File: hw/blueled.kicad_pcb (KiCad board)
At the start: 2 copper layers, 54 x 85.6 mm, 58 parts, among them J1 Barrel_Jack, J2 LED Strip, J3 ICSP, J4 Screw_Terminal_01x02, Q1 Q_PMOS_SDG, Q2 Q_PNP_EBC, SW2 PUSH, U1 ATmega328P-AU, U2 HC-05, U3 AMS1117-3.3, U4 AT25SF081, U5 LM25085MM, X1 CSTCE

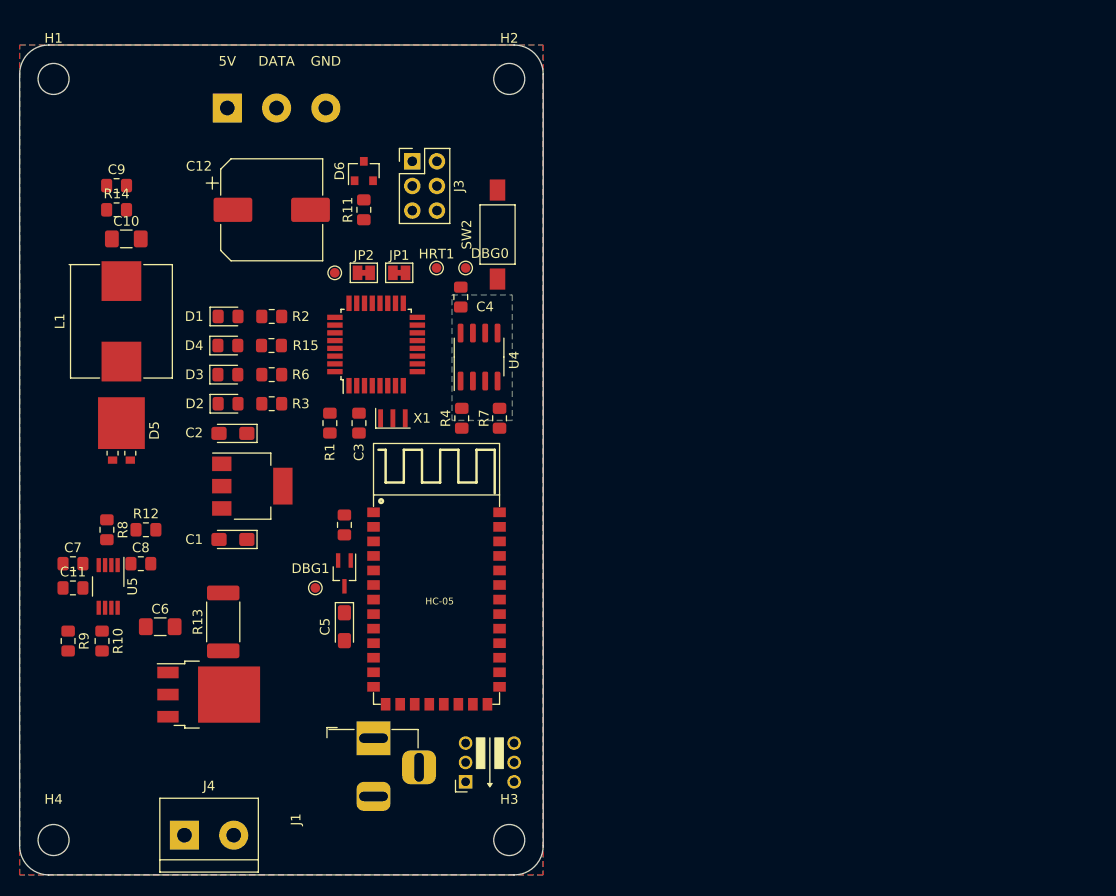
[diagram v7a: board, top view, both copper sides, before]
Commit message: add(hw): a lot of progress in layouting + bug fixes
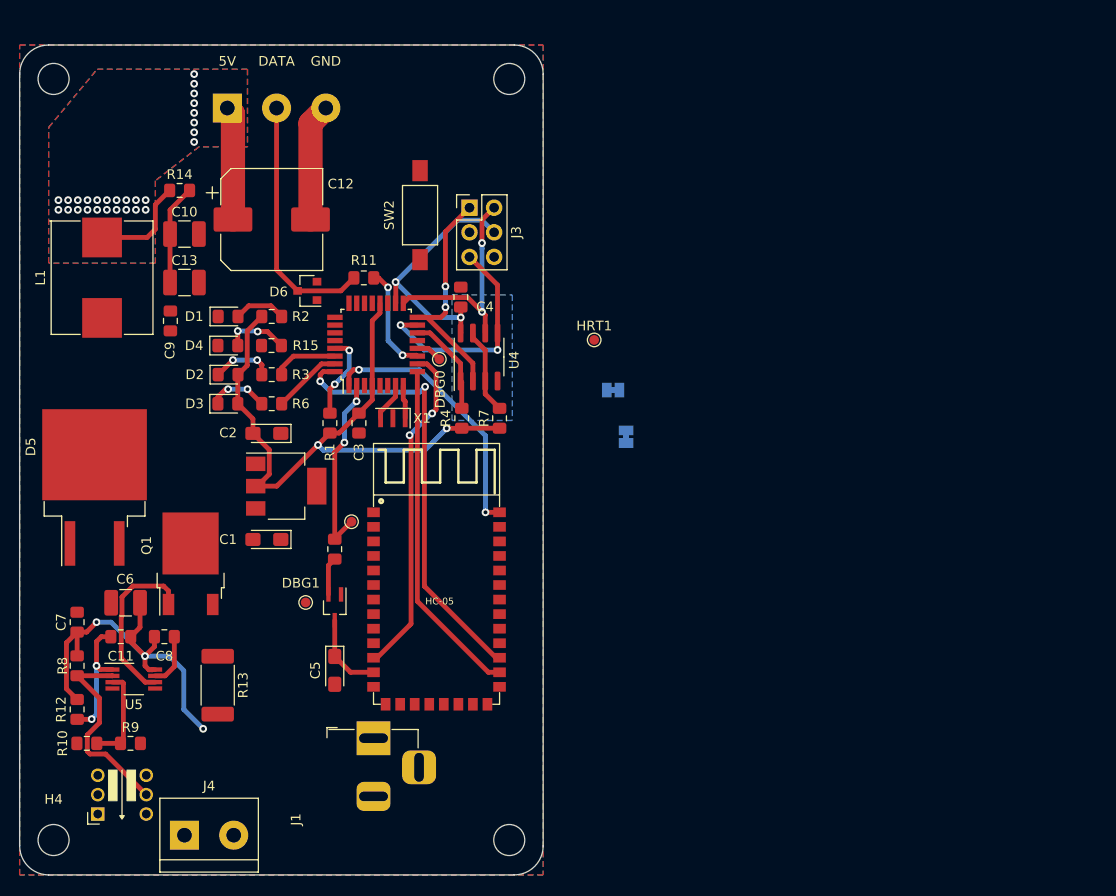
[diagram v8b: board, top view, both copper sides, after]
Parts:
- added C13: 47uF, Capacitor_SMD:C_1210_3225Metric_Pad1.42x2.65mm_HandSolder, F.Cu at (137.0, 87.5)
- C10: value 100uF -> 47uF; footprint Capacitor_SMD:C_1206_3216Metric_Pad1.42x1.75mm_HandSolder -> Capacitor_SMD:C_1210_3225Metric_Pad1.42x2.65mm_HandSolder
- C6: footprint Capacitor_SMD:C_1206_3216Metric_Pad1.42x1.75mm_HandSolder -> Capacitor_SMD:C_1210_3225Metric_Pad1.42x2.65mm_HandSolder
- C9: value 0.1uF -> 4700pF
- D5: footprint Diode_SMD:D_Powermite3 -> Package_TO_SOT_SMD:TO-263-3_TabPin2
- JP1, JP2: moved to B.Cu
- R14: value 10k -> 0.27
- moved S1 38.1 mm to (130.6, 140.3)
- moved JP2 31.9 mm to (182.6, 103.4), turned to 90 degrees
- moved DBG2 25.7 mm to (154.2, 112.2)
- moved JP1 25.2 mm to (181.2, 98.6)
- moved R12 19.8 mm to (125.9, 131.5), turned to 90 degrees
- moved HRT1 17.9 mm to (179.3, 93.4)
- moved C9 15.0 mm to (135.6, 91.5), turned to 90 degrees
- moved R8 14.4 mm to (125.9, 127.0)
- moved D6 13.7 mm to (149.7, 88.4), turned to 180 degrees
- moved Q1 13.6 mm to (137.6, 116.5), turned to 90 degrees
- moved R9 12.4 mm to (131.4, 135.0), turned to 0 degrees
- moved R10 10.7 mm to (126.9, 135.0), turned to 0 degrees
- moved U5 9.91 mm to (131.8, 128.4), turned to 0 degrees
- moved DBG0 9.79 mm to (163.3, 95.4)
- moved SW2 8.24 mm to (161.3, 80.5)
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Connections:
- C12 pad 1: (no net) -> +5V
- Q1 pad 1: Net-(D5-Pad1) -> Net-(Q1-Pad1)
- Q1 pad 2: Net-(Q1-Pad2) -> Net-(D5-Pad1)
- R13 pad 1: Net-(Q1-Pad2) -> Net-(Q1-Pad1)
- U5 pad 5: Net-(Q1-Pad2) -> Net-(Q1-Pad1)
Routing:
- net +3V3: track 0.00 -> 92.9 mm, vias 0 -> 4
- net /HC-STATE: track 0.00 -> 45.3 mm, vias 0 -> 2
- net /VINJACK: track 0.00 -> 41.8 mm, vias 0 -> 3
- net /HC-DISCNCT: track 0.00 -> 35.2 mm
- net /HC-RESET: track 0.00 -> 34.8 mm, vias 0 -> 2
- net /HC-ATMODE: track 0.00 -> 27.6 mm, vias 0 -> 2
- net /DATA: track 0.00 -> 26.1 mm
- net /MISO: track 0.00 -> 24.5 mm, vias 0 -> 2
- net /MOSI: track 0.00 -> 23.7 mm, vias 0 -> 2
- net /SCK: track 0.00 -> 22.6 mm, vias 0 -> 2
- net +5V: track 0.00 -> 22.2 mm, vias 0 -> 27
- net /SHUTDOWN: track 0.00 -> 20.8 mm
- net /~HC-POWER-EN: track 0.00 -> 19.3 mm, vias 0 -> 2
- net Net-(Q1-Pad3): track 0.00 -> 17.7 mm
- net Net-(C11-Pad2): track 0.00 -> 13.2 mm, vias 0 -> 2
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- added copper zone on B.Cu, net +5V
- added copper zone on F.Cu, net +5V
